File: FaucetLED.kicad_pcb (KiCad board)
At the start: 2 copper layers, 34.5 x 28.4 mm, 40 parts, among them P1 CONN_01X03, P2 CONN_01X02, P3 CONN_01X02, P4 CONN_01X03, P5 CONN_01X02, P6 CONN_01X01, Q1 BSS138, Q2 BSS138, Q3 BSS138, U1 TLV70033DDC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

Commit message: Add name and version to silkscreen.
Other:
- board text added: "Faucet LED v2.0 Nick Graumann"
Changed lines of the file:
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@@
     (area 101.524999 76.124999 136.219001 104.723001)
     (thickness 1.6)
-    (drawings 4)
+    (drawings 5)
     (tracks 298)
     (zones 0)
@@
       (net 20 "Net-(BT1-Pad1)"))
   )
+  (gr_text "Faucet LED v2.0\nNick Graumann" (at 119.7864 82.1944) (layer B.SilkS)
+    (effects (font (size 0.762 0.762) (thickness 0.127)) (justify mirror))
+  )
   (gr_line (start 136.144 76.2) (end 101.6 76.2) (layer Edge.Cuts) (width 0.15))

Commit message: Update to Kicad 4.0.5, re-import libraries.
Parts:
- removed P3: CONN_01X02, Pin_Headers:Pin_Header_Straight_1x01_Pitch2.54mm
- BT2: footprint Pin_Headers:Pin_Header_Angled_1x02_Pitch2.00mm -> Connectors_JST:JST_PH_S2B-PH-K_02x2.00mm_Angled
- P1: footprint Pin_Headers:Pin_Header_Straight_1x04_Pitch2.54mm -> Connectors_JST:JST_PH_S4B-PH-K_04x2.00mm_Angled
- P2: footprint Pin_Headers:Pin_Header_Straight_1x02_Pitch2.54mm -> Connectors_JST:JST_PH_S4B-PH-K_04x2.00mm_Angled
- R1: value 100R -> 130R
- turned BT2 to 270 degrees

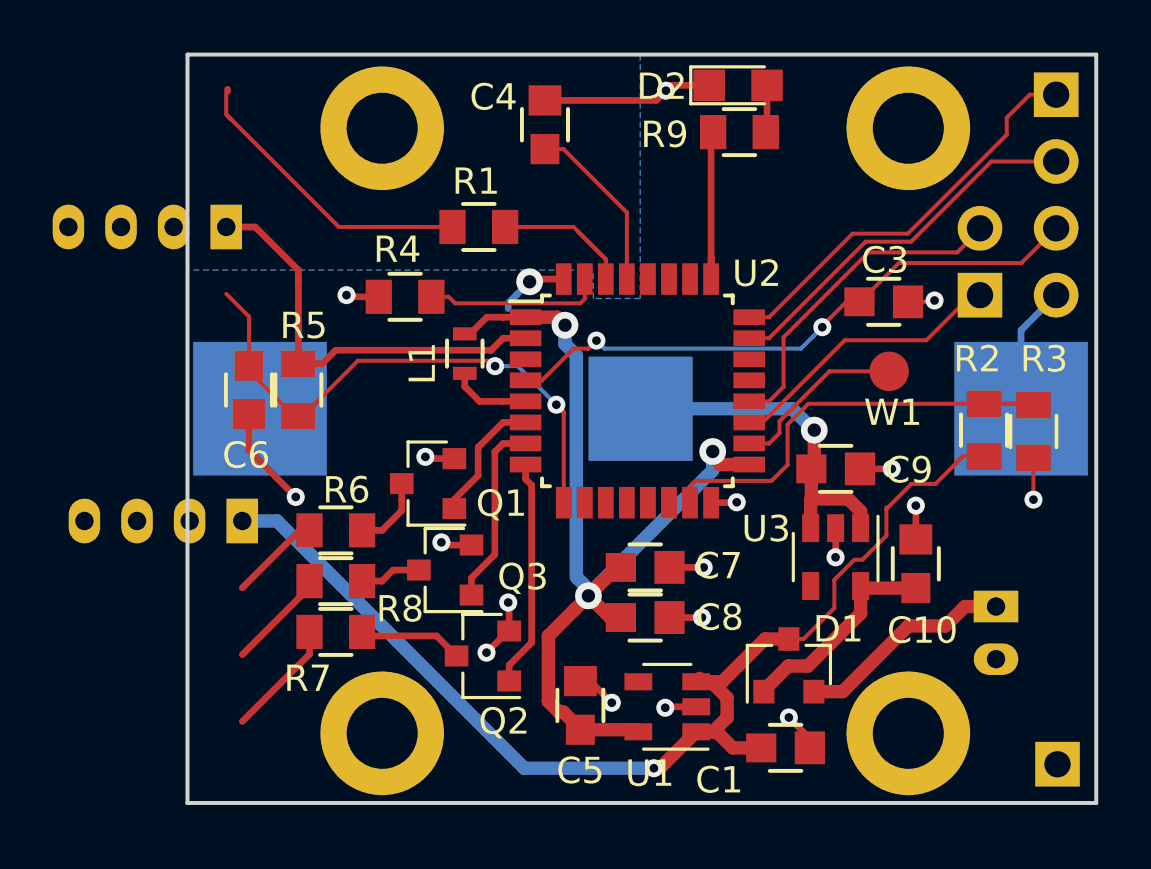
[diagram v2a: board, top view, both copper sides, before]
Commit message: Fix coin cell holder to have GND pad in middle.
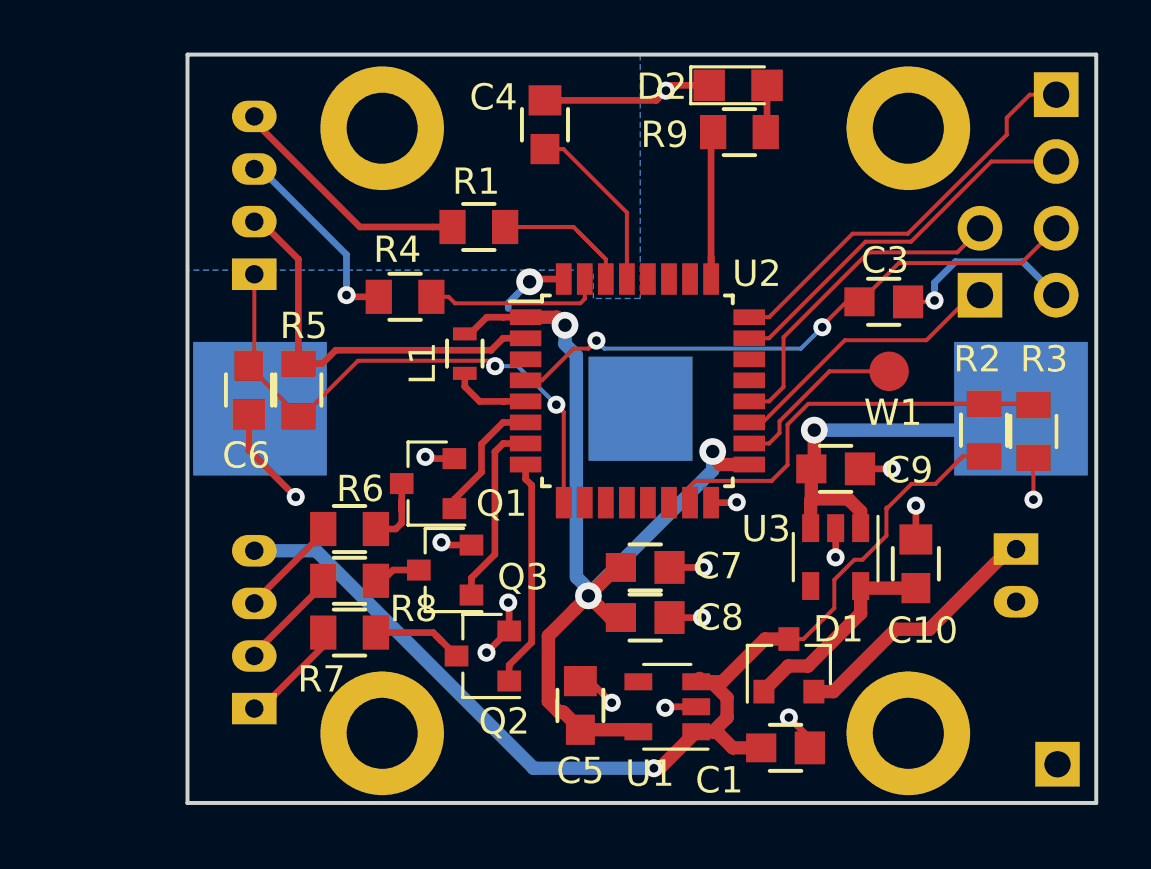
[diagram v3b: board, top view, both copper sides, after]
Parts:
- BT1: footprint components:Keystone_3020_CR2016x2 -> components:Keystone_3020_2x2016-CoinCell
- moved P1 7.15 mm to (104.1, 101.1), turned to 90 degrees
- moved BT2 2.31 mm to (133.1, 95.0)
- moved P2 2.09 mm to (104.1, 84.5), turned to 90 degrees
- moved R6 0.52 mm to (107.8, 94.2)
- moved R7 0.52 mm to (107.8, 98.2)
- moved R8 0.52 mm to (107.8, 96.2)
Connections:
- P1 pad 1: +BATT -> /LED_B_CONN
- P1 pad 2: /LED_R_CONN -> /LED_G_CONN
- P1 pad 3: /LED_G_CONN -> /LED_R_CONN
- P1 pad 4: /LED_B_CONN -> +BATT
- P2 pad 1: /THERM_SW -> /THERM_SENSE
- P2 pad 2: /THERM_SENSE -> /THERM_SW
- P2 pad 3: /TSC_IN -> GND
- P2 pad 4: GND -> /TSC_IN
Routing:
- net GND: track 37.8 -> 45.5 mm
- net /TSC_IN: track 11.4 -> 9.39 mm
- net Net-(BT2-Pad1): track 8.26 -> 9.93 mm
- net Net-(BT1-Pad1): track 13.6 -> 15.1 mm
- net +BATT: track 42.8 -> 41.8 mm
- net /THERM_SW: track 16.2 -> 15.3 mm
- net Net-(Q3-Pad3): track 2.33 -> 1.58 mm
- net /THERM_SENSE: track 21.1 -> 21.8 mm
- net /LED_R_CONN: track 3.46 -> 4.16 mm

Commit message: Move uC up a bit for more room, increase center battery pad size.
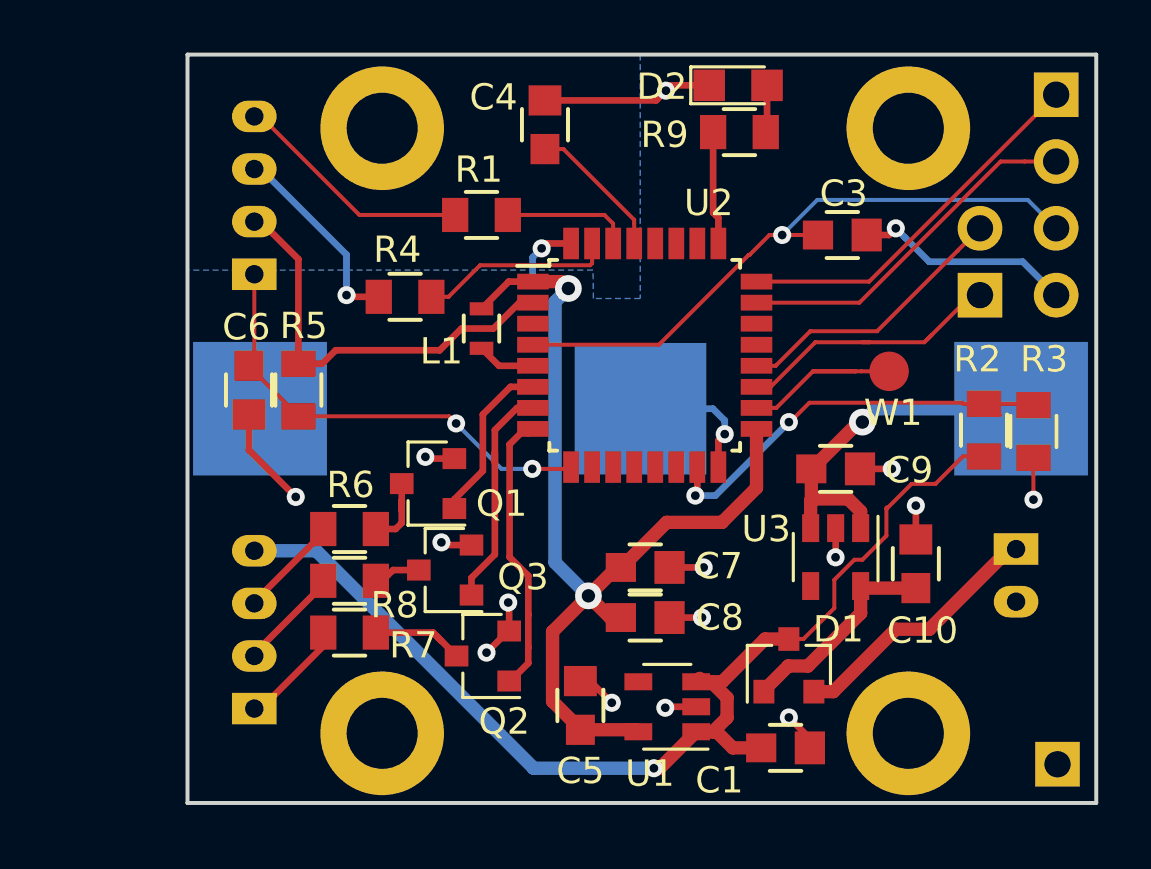
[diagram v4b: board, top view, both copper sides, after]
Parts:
- moved C3 2.99 mm to (126.5, 83.1)
- moved U2 1.38 mm to (119.0, 87.6)
- moved L1 1.14 mm to (112.8, 86.6)
- moved R1 0.47 mm to (112.8, 82.3)
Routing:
- net GND: track 45.5 -> 50.9 mm
- net /THERM_SENSE: track 21.8 -> 18.0 mm
- net /LED_B: track 8.68 -> 11.0 mm
- net /LED_DBG: track 6.37 -> 4.32 mm
- net /UART_RX: track 12.6 -> 10.7 mm
- net /LED_G: track 7.11 -> 8.83 mm
- net Net-(R1-Pad2): track 6.57 -> 4.89 mm
- net /LED_R: track 4.90 -> 6.36 mm
- net /TSC_SAMPLING: track 6.67 -> 5.43 mm
- net /SWCLK: track 15.6 -> 14.3 mm
- net /RESET: track 22.8 -> 24.0 mm, vias 2 -> 1
- net Net-(BT1-Pad1): track 15.1 -> 14.1 mm
- net +3V3: track 35.7 -> 36.8 mm, vias 3 -> 2
- net /SWDIO: track 14.5 -> 13.6 mm
- net /THERM_SW: track 15.3 -> 16.1 mm
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
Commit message: Add combo footprint for both QFN32 and LQFP32.
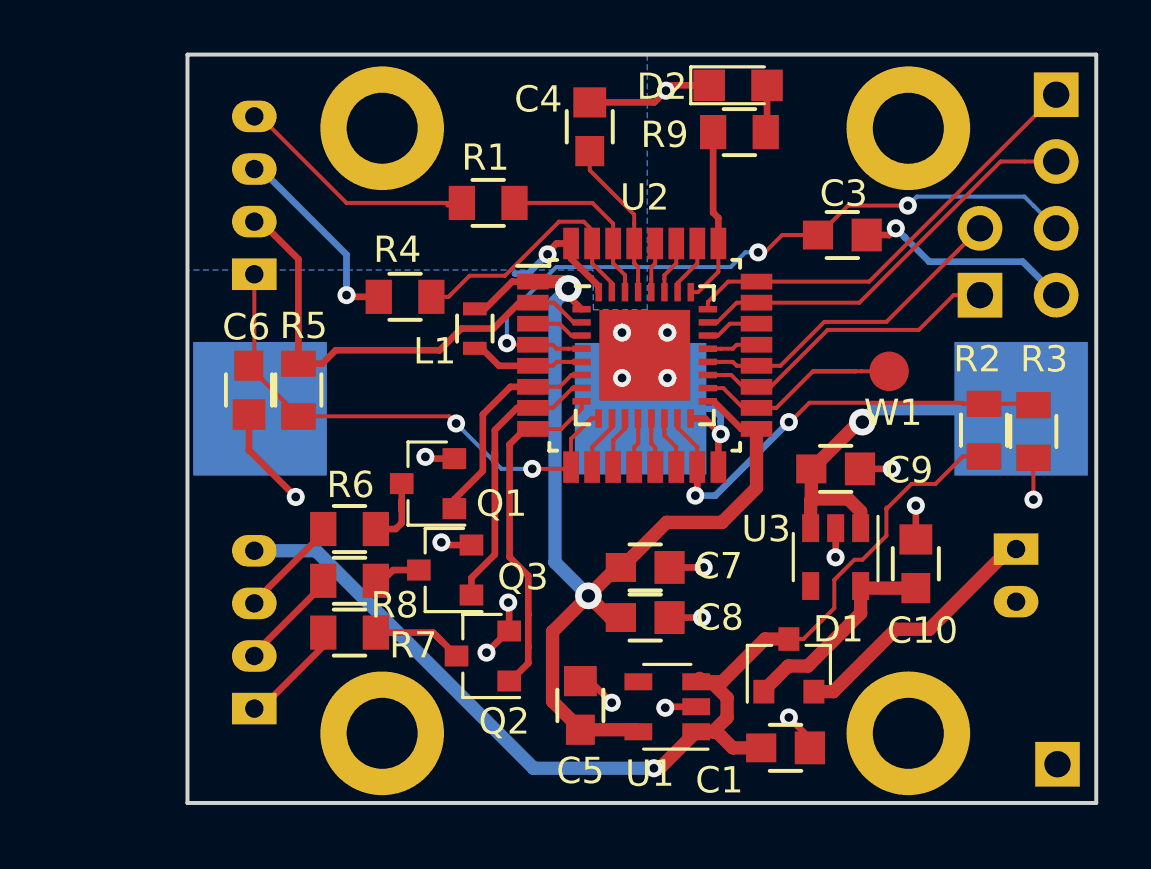
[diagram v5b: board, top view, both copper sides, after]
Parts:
- U2: footprint Housings_QFP:LQFP-32_7x7mm_Pitch0.8mm -> components:LQFP-32_7x7mm_Pitch0.8mm_QFN-32-1EP_5x5mm_Pitch0.5mm-Combo
- moved C4 1.70 mm to (116.9, 78.9)
- moved R1 0.52 mm to (113.0, 81.8)
- moved L1 0.25 mm to (112.5, 86.6)
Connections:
- U2 pad 10: (no net) -> Net-(U2-Pad10)
- U2 pad 11: (no net) -> Net-(U2-Pad11)
- U2 pad 12: (no net) -> Net-(U2-Pad12)
- U2 pad 13: (no net) -> Net-(U2-Pad13)
- U2 pad 14: (no net) -> Net-(U2-Pad14)
- U2 pad 21: (no net) -> Net-(U2-Pad21)
- U2 pad 22: (no net) -> Net-(U2-Pad22)
- U2 pad 26: (no net) -> Net-(U2-Pad26)
- U2 pad 27: (no net) -> Net-(U2-Pad27)
- U2 pad 28: (no net) -> Net-(U2-Pad28)
- U2 pad 3: (no net) -> Net-(U2-Pad3)
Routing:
- net GND: track 50.9 -> 59.6 mm, vias 19 -> 23
- net +3V3: track 36.8 -> 40.0 mm
- net /RESET: track 24.0 -> 27.2 mm, vias 1 -> 3
- net Net-(R4-Pad1): track 7.39 -> 10.1 mm
- net /LED_DBG: track 4.32 -> 6.76 mm
- net /SWCLK: track 14.3 -> 16.8 mm
- net /LED_B: track 11.0 -> 13.4 mm
- net /THERM_SENSE: track 18.0 -> 20.4 mm
- net Net-(U2-Pad26): track 0.00 -> 2.16 mm
- net /SWDIO: track 13.6 -> 15.8 mm
- net /MCO: track 7.24 -> 9.40 mm
- net /THERM_SW: track 16.1 -> 18.3 mm
- net /BATT_2: track 16.4 -> 18.5 mm
- net Net-(U2-Pad10): track 0.00 -> 2.16 mm
- net /LED_G: track 8.83 -> 11.0 mm
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
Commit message: Added more bypass caps.
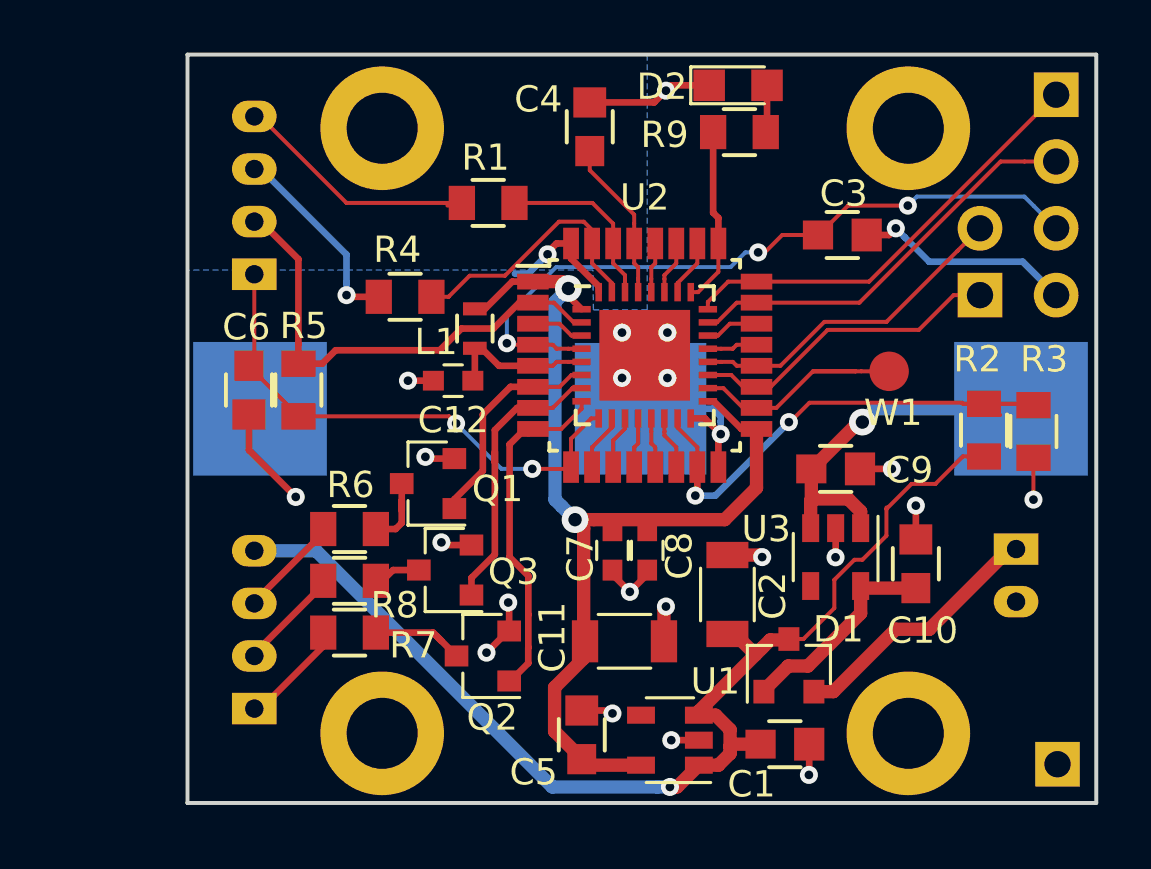
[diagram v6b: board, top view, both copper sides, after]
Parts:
- added C11: 10u, Capacitors_SMD:C_1206, F.Cu at (118.2, 98.5)
- added C12: 100n, Capacitors_SMD:C_0603, F.Cu at (111.7, 88.6)
- added C2: 100u, Capacitors_SMD:C_1206, F.Cu at (122.1, 96.7)
- C7: value 0.1u -> 100n; footprint components:C_0603_0805 -> Capacitors_SMD:C_0603
- C8: footprint components:C_0603_0805 -> Capacitors_SMD:C_0603
- moved C8 2.55 mm to (119.1, 95.0), turned to 270 degrees
- moved C7 1.40 mm to (117.8, 95.0), turned to 270 degrees
- moved U1 1.27 mm to (119.9, 102.3)
- moved C5 1.12 mm to (116.6, 102.1)
- moved C1 0.14 mm to (124.3, 102.4)
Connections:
- net Net-(L1-Pad2) renamed +3.3VA
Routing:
- net GND: track 59.6 -> 62.2 mm, vias 23 -> 25
- net +BATT: track 41.8 -> 43.5 mm
- net +3.3VA: track 4.14 -> 5.40 mm

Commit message: Move around caps for better layout.
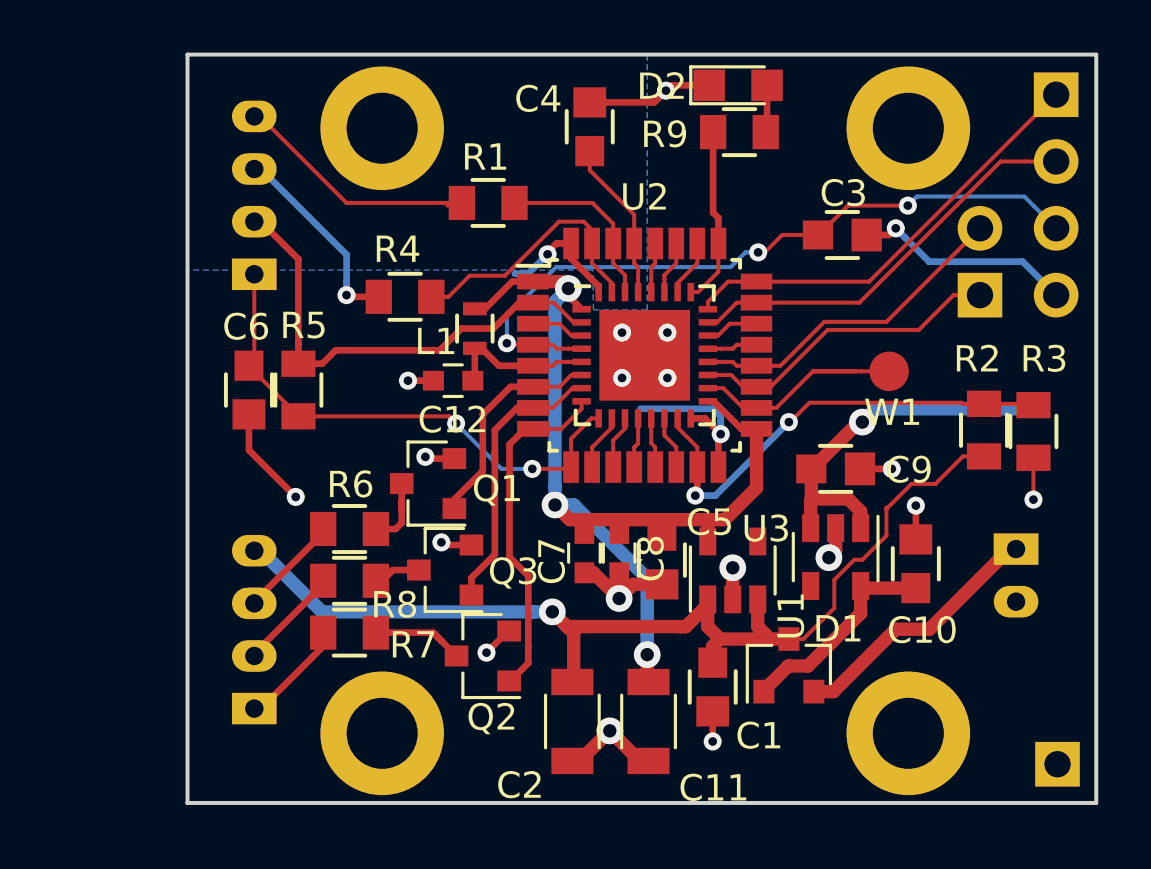
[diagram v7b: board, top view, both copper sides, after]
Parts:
- removed BT1: CR2016x2, components:Keystone_3020_2x2016-CoinCell
- moved C2 7.62 mm to (116.2, 101.5), turned to 270 degrees
- moved C5 7.31 mm to (119.6, 95.4), turned to 270 degrees
- moved U1 6.88 mm to (122.3, 95.8), turned to 90 degrees
- moved C1 3.50 mm to (121.6, 100.2), turned to 270 degrees
- moved C11 3.18 mm to (119.1, 101.5), turned to 270 degrees
- moved C7 1.07 mm to (116.7, 95.1)
- moved C8 1.07 mm to (118.0, 95.1)
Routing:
- net +BATT: track 43.5 -> 39.7 mm
- net +3V3: track 39.8 -> 37.7 mm, vias 2 -> 3
- net GND: track 62.2 -> 63.4 mm, vias 25 -> 22
